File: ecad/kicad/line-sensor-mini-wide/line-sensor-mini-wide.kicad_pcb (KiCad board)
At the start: 2 copper layers, 28.7 x 81.3 mm, 37 parts, among them J1 SENSORS, Q1 BC337, Q2 BC337, Q3 BPW85C, Q4 BPW85C, Q5 BPW85C, Q6 BPW85C, Q7 BPW85C, Q8 BPW85C

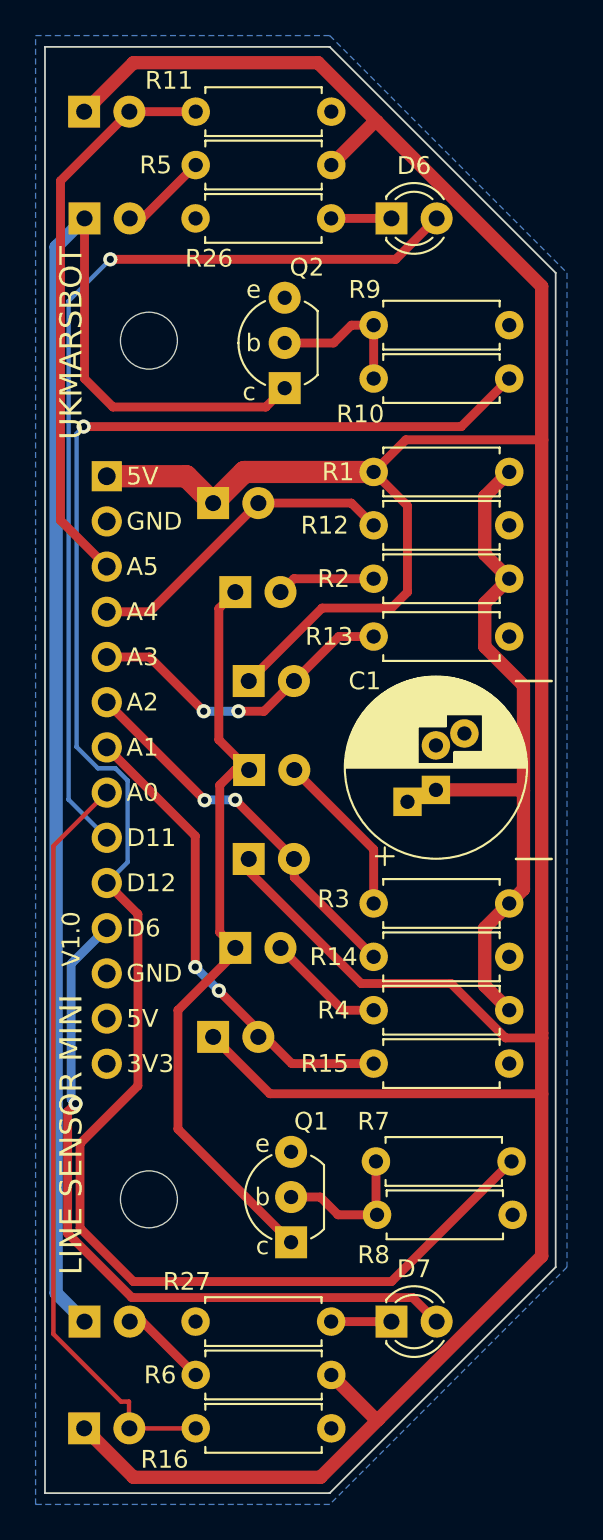
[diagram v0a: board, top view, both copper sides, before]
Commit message: re-route mini wide line sensor
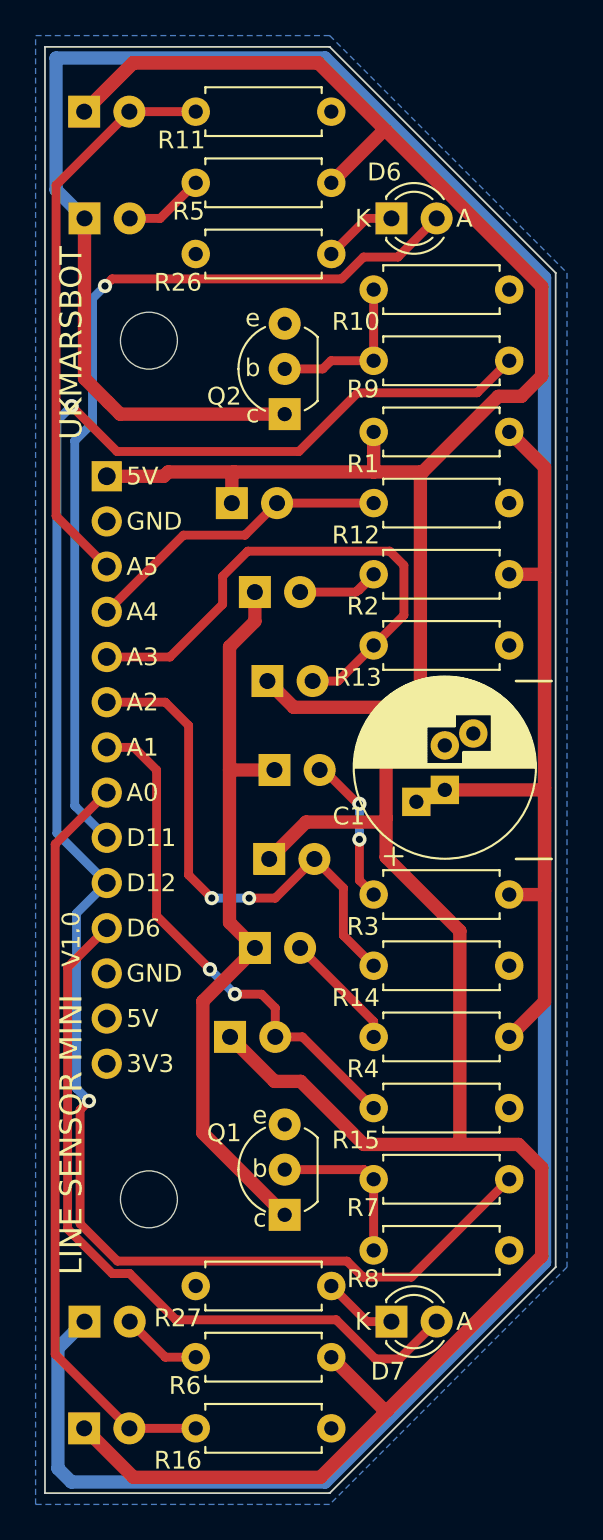
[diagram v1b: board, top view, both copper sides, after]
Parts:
- moved R1 7.95 mm to (157.0, 86.0), turned to 0 degrees
- moved R26 7.87 mm to (147.0, 76.0), turned to 0 degrees
- moved R27 7.87 mm to (147.0, 134.0), turned to 0 degrees
- moved R7 7.81 mm to (157.0, 128.0), turned to 0 degrees
- moved R6 7.69 mm to (147.0, 138.0), turned to 0 degrees
- moved R9 7.69 mm to (157.0, 82.0), turned to 0 degrees
- moved R3 7.64 mm to (157.0, 112.0), turned to 0 degrees
- moved R15 2.50 mm to (157.0, 124.0)
- moved R8 2.01 mm to (157.0, 132.0)
- moved R10 2.00 mm to (157.0, 78.0)
- moved Q1 1.58 mm to (152.0, 130.0)
- moved R4 1.50 mm to (157.0, 120.0)
- moved Q2 1.46 mm to (152.0, 85.0)
- moved D3 1.43 mm to (151.4, 105.0)
- moved R12 1.25 mm to (157.0, 90.0)
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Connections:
- D5 pad 2: Net-(D5-Pad2) -> Net-(R6-Pad1)
- R1 pad 1: /5V_EMITTERS -> 5V
- R1 pad 2: 5V -> /5V_EMITTERS
- R26 pad 1: Net-(D6-Pad1) -> GND
- R26 pad 2: GND -> Net-(D6-Pad1)
- R27 pad 1: Net-(D7-Pad1) -> GND
- R27 pad 2: GND -> Net-(D7-Pad1)
- R3 pad 1: /5V_EMITTERS -> Net-(D3-Pad2)
- R3 pad 2: Net-(D3-Pad2) -> /5V_EMITTERS
- R6 pad 1: 5V -> Net-(R6-Pad1)
- R6 pad 2: Net-(D5-Pad2) -> 5V
- R7 pad 1: D12_EMITTERS -> Net-(Q1-Pad2)
- R7 pad 2: Net-(Q1-Pad2) -> D12_EMITTERS
- R9 pad 1: D12_EMITTERS -> Net-(Q2-Pad2)
- R9 pad 2: Net-(Q2-Pad2) -> D12_EMITTERS
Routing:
- net /marker_emitters: track 84.7 -> 160.7 mm
- net A3_LINE_3: track 18.0 -> 29.9 mm, vias 2 -> 0
- net A2_LINE_2: track 21.6 -> 29.4 mm
- net 5V: track 211.6 -> 205.5 mm
- net /5V_EMITTERS: track 39.3 -> 45.4 mm
- net Net-(D5-Pad2): track 4.95 -> 0.00 mm
- net Net-(R6-Pad1): track 0.00 -> 4.54 mm
- net A0_START_MARKER: track 42.7 -> 46.6 mm
- net Net-(D2-Pad2): track 5.55 -> 8.99 mm
- net A1_LINE_1: track 26.7 -> 29.2 mm
- net D6_LED_RIGHT: track 41.1 -> 42.4 mm, vias 1 -> 0
- net /sensor_emitters: track 43.1 -> 41.7 mm
- net D12_EMITTERS: track 102.9 -> 104.1 mm, vias 1 -> 2
- net Net-(D3-Pad2): track 9.35 -> 8.22 mm, vias 0 -> 2
- net D11_LED_LEFT: track 53.7 -> 52.7 mm
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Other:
- board text added: "A"
- board text added: "K"

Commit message: improved BOM mini wide line sensor
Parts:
- D1, D2, D3, D4, D5: value LED -> L-934F3C
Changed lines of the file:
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@@
       (effects (font (size 1 1) (thickness 0.15)) (justify mirror))
     )
-    (fp_text value "LED" (at 4.75 3) (layer "B.Fab")
+    (fp_text value "L-934F3C" (at 1.95 3.3) (layer "B.Fab")
       (effects (font (size 1 1) (thickness 0.15)) (justify mirror))
     )
@@
       (effects (font (size 1 1) (thickness 0.15)) (justify mirror))
     )
-    (fp_text value "LED" (at 5.025 1.27) (layer "B.Fab")
+    (fp_text value "L-934F3C" (at 1.675 -1.8) (layer "B.Fab")
       (effects (font (size 1 1) (thickness 0.15)) (justify mirror))
     )
@@
       (effects (font (size 1 1) (thickness 0.15)) (justify mirror))
     )
-    (fp_text value "LED" (at 5.25 1.25) (layer "B.Fab")
+    (fp_text value "L-934F3C" (at 1.175 -1.7) (layer "B.Fab")
       (effects (font (size 1 1) (thickness 0.15)) (justify mirror))
     )
@@
       (effects (font (size 1 1) (thickness 0.15)) (justify mirror))
     )
-    (fp_text value "LED" (at 1.27 -2.96) (layer "B.Fab")
+    (fp_text value "L-934F3C" (at 2.05 -3.2) (layer "B.Fab")
       (effects (font (size 1 1) (thickness 0.15)) (justify mirror))
     )
@@
       (effects (font (size 1 1) (thickness 0.15)) (justify mirror))
     )
-    (fp_text value "LED" (at 5.2 1.5) (layer "B.Fab")
-      (effects (font (size 1 1) (thickness 0.15)) (justify mirror))
-    )
+    (fp_text value "L-934F3C" (at 1.175 -1.8) (layer "B.Fab")
+      (effects (font (size 1 1) (thickness 0.15)) (justify mirror))
+    )
